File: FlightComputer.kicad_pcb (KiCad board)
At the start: 2 copper layers, 73.7 x 73.7 mm, 88 parts, among them J1 B3B-XH-A, J3 DM3D-SF, J4 12401832E402A, U1 AP62150WU-7TSOT26-WU_DIO, U2 TPS2121RUXR, U4 RP2350_60QFN, Y1 ABM8-272-T3

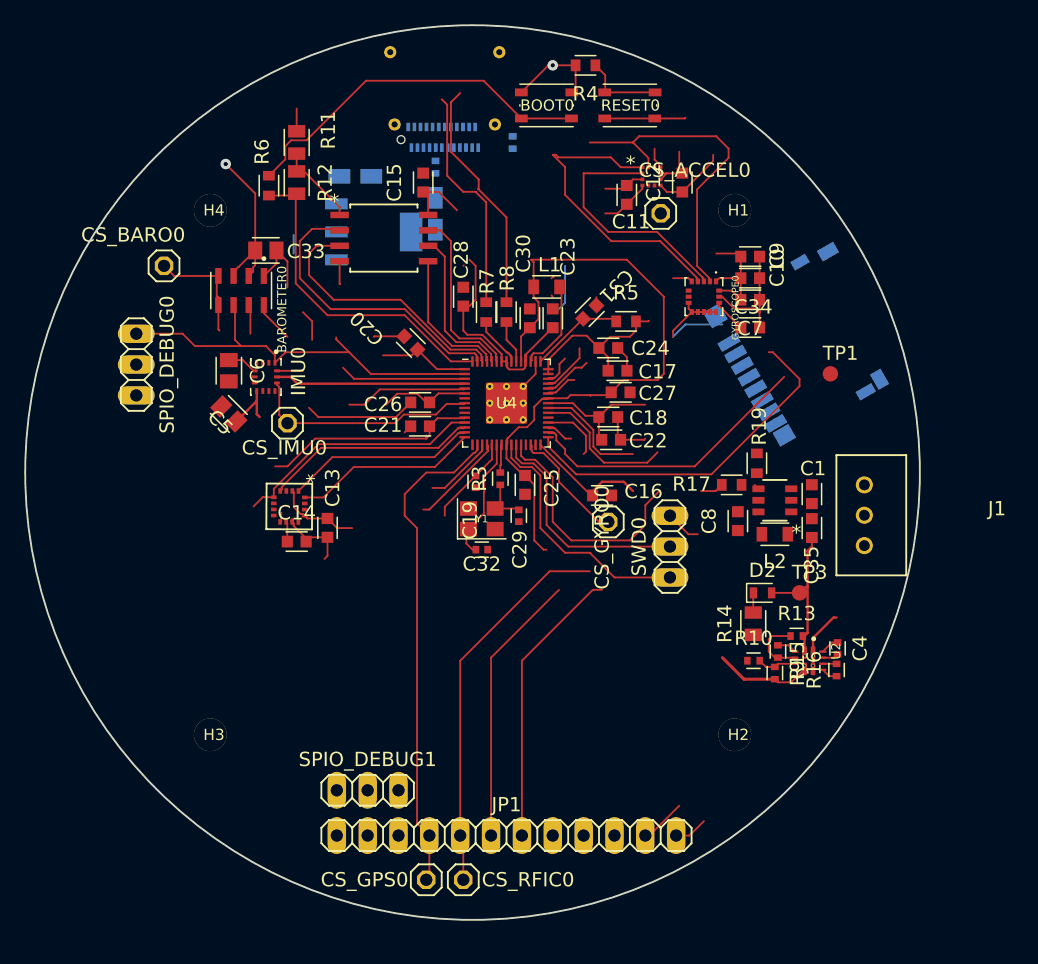
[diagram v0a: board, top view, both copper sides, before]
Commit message: fix: derived + added missing vals for passives, cleaned up stuff
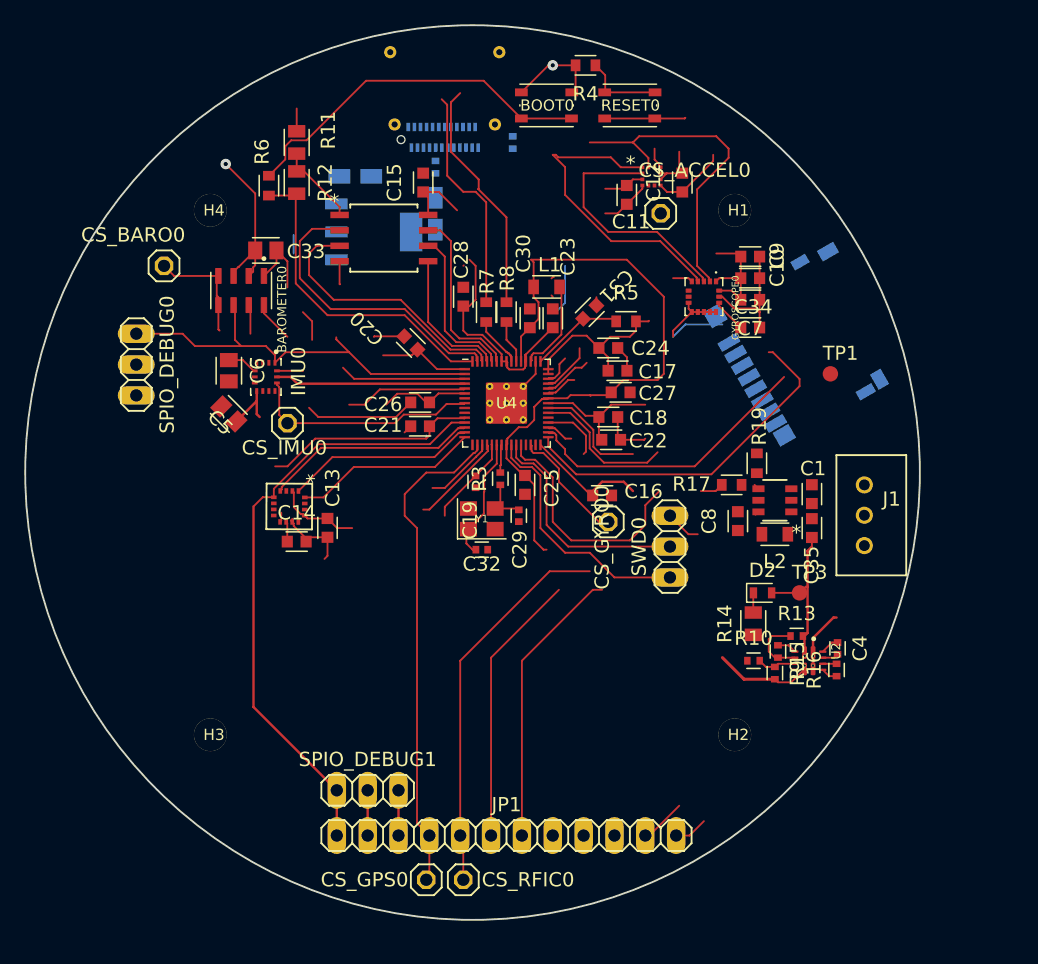
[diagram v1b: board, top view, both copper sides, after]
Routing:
- net MISO1: track 20.7 -> 50.6 mm
- net MOSI1: track 15.2 -> 18.9 mm
- net SCLK1: track 15.7 -> 19.4 mm
- added copper zone on In2.Cu, net +3.3V
- added copper zone on In1.Cu, net GND
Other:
- copper layers 2 -> 4
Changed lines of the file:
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@@
 	(layers
 		(0 "F.Cu" signal)
+		(4 "In1.Cu" signal)
+		(6 "In2.Cu" signal)
 		(2 "B.Cu" signal)
 		(9 "F.Adhes" user "F.Adhesive")
@@
 	)
 	(setup
+		(stackup
+			(layer "F.SilkS"
+				(type "Top Silk Screen")
+			)
+			(layer "F.Paste"
+				(type "Top Solder Paste")
+			)
+			(layer "F.Mask"
+				(type "Top Solder Mask")
+				(thickness 0.01)
+			)
+			(layer "F.Cu"
+				(type "copper")
+				(thickness 0.035)
+			)
+			(layer "dielectric 1"
+				(type "prepreg")
+				(thickness 0.1)
+				(material "FR4")
+				(epsilon_r 4.5)
+				(loss_tangent 0.02)
+			)
+			(layer "In1.Cu"
+				(type "copper")
+				(thickness 0.035)
+			)
+			(layer "dielectric 2"
+				(type "core")
+				(thickness 1.24)
+				(material "FR4")
+				(epsilon_r 4.5)
+				(loss_tangent 0.02)
+			)
+			(layer "In2.Cu"
+				(type "copper")
+				(thickness 0.035)
+			)
+			(layer "dielectric 3"
+				(type "prepreg")
+				(thickness 0.1)
+				(material "FR4")
+				(epsilon_r 4.5)
+				(loss_tangent 0.02)
+			)
+			(layer "B.Cu"
+				(type "copper")
+				(thickness 0.035)
+			)
+			(layer "B.Mask"
+				(type "Bottom Solder Mask")
+				(thickness 0.01)
+			)
+			(layer "B.Paste"
+				(type "Bottom Solder Paste")
+			)
+			(layer "B.SilkS"
+				(type "Bottom Silk Screen")
+			)
+			(copper_finish "None")
+			(dielectric_constraints no)
+		)
 		(pad_to_mask_clearance 0)
 		(allow_soldermask_bridges_in_footprints no)
@@
 		(at 180.7591 106.0196 -90)
 		(property "Reference" "J1"
-			(at 1.27 -10.922 0)
+			(at 0.4804 -2.2409 0)
 			(unlocked yes)
 			(layer "F.SilkS")
@@
 		(descr "Chip, 2.00 X 1.25 X 1.10 mm body\n\nChip package with body size 2.00 X 1.25 X 1.10 mm")
 		(property "Reference" "C5"
-			(at 0.000001 -1.681701 -45)
+			(at 0.000001 -1.681701 315)
 			(unlocked yes)
 			(layer "F.SilkS")
@@
 		)
 		(property "Value" ""
-			(at 0.000001 1.681701 -45)
+			(at 0.000001 1.681701 315)
 			(unlocked yes)
 			(layer "F.Fab")
@@
 		(descr "Chip, 1.60 X 0.80 X 0.85 mm body\n\nChip package with body size 1.60 X 0.80 X 0.85 mm")
 		(property "Reference" "C31"
-			(at -3.053284 0.653166 -135)
+			(at -3.053284 0.653166 225)
 			(unlocked yes)
 			(layer "F.SilkS")
@@
 		)
 		(property "Value" ""
-			(at 0.000003 1.681701 -135)
+			(at 0.000003 1.681701 225)
 			(unlocked yes)
 			(layer "F.Fab")
@@
 		)
 		(property "Value" "KX134-1211LGA12_2X2X0P9_ROM"
-			(at -1.7288 0.635 0)
+			(at -3.2331 0.635 0)
 			(unlocked yes)
 			(layer "F.Fab")
@@
 		(at 133.41245 107.7976 -90.3)
 		(property "Reference" "MAGNETOMETER0"
-			(at -3.271195 0.63503 -179.7)
+			(at -3.271195 0.63503 180.3)
 			(unlocked yes)
 			(layer "F.Fab")
@@
 		)
 		(property "Value" "MMC5983MAMMC5983MA_MEM"
-			(at -1.728787 0.635029 -179.7)
+			(at -1.728787 0.635029 180.3)
 			(unlocked yes)
 			(layer "F.Fab")
@@
 		(descr "Chip, 1.60 X 0.80 X 0.85 mm body\n\nChip package with body size 1.60 X 0.80 X 0.85 mm")
 		(property "Reference" "C20"
-			(at -3.412499 1.012376 -225)
+			(at -3.412499 1.012376 135)
 			(unlocked yes)
 			(layer "F.SilkS")
@@
 		)
 		(property "Value" ""
-			(at 0.000001 1.681699 -225)
+			(at 0.000001 1.681699 135)
 			(unlocked yes)
 			(layer "F.Fab")
@@
 		)
 		(property "Datasheet" ""
-			(at 0 0 -60)
+			(at 0 0 300)
 			(layer "B.Fab")
 			(hide yes)
@@
 		)
 		(property "Description" ""
-			(at 0 0 -60)
+			(at 0 0 300)
 			(layer "B.Fab")
 			(hide yes)
@@
 		(descr "Chip, 1.05 X 0.54 X 0.40 mm body\n\nChip package with body size 1.05 X 0.54 X 0.40 mm")
 		(property "Reference" "R18"
-			(at -2.794 0.508 -90)
+			(at -2.794 0.508 270)
 			(unlocked yes)
 			(layer "B.SilkS")
@@
 		)
 		(property "Value" "5.1k"
-			(at 0 -2.54 -90)
+			(at 0 -2.54 270)
 			(unlocked yes)
 			(layer "B.Fab")
@@
 		)
 		(property "Datasheet" ""
-			(at 0 0 -90)
+			(at 0 0 270)
 			(layer "B.Fab")
 			(hide yes)
@@
 		)
 		(property "Description" ""
-			(at 0 0 -90)
+			(at 0 0 270)
 			(layer "B.Fab")
 			(hide yes)
@@
 		(descr "Chip, 1.05 X 0.54 X 0.40 mm body\n\nChip package with body size 1.05 X 0.54 X 0.40 mm")
 		(property "Reference" "R20"
-			(at -3.302 0.508 -90)
+			(at -3.302 0.508 270)
 			(unlocked yes)
 			(layer "B.SilkS")
@@
 		)
 		(property "Value" "5.1k"
-			(at 0 -2.54 -90)
+			(at 0 -2.54 270)
 			(unlocked yes)
 			(layer "B.Fab")
@@
 		)
 		(property "Datasheet" ""
-			(at 0 0 -90)
+			(at 0 0 270)
 			(layer "B.Fab")
 			(hide yes)
@@
 		)
 		(property "Description" ""
-			(at 0 0 -90)
+			(at 0 0 270)
 			(layer "B.Fab")
 			(hide yes)
@@
 		(descr "Molded Body, 3.20 X 1.60 X 1.80 mm body\n\nMolded Body package with body size 3.20 X 1.60 X 1.80 mm")
 		(property "Reference" "C3"
-			(at 1.524 -1.27 -90)
+			(at 1.524 -1.27 270)
 			(unlocked yes)
 			(layer "B.SilkS")
@@
 		)
 		(property "Value" "100u"
-			(at 0 -2.54 -90)
+			(at 0 -2.54 270)
 			(unlocked yes)
 			(layer "B.Fab")
@@
 		)
 		(property "Datasheet" ""
-			(at 0 0 -90)
+			(at 0 0 270)
 			(layer "B.Fab")
 			(hide yes)
@@
 		)
 		(property "Description" ""
-			(at 0 0 -90)
+			(at 0 0 270)
 			(layer "B.Fab")
 			(hide yes)
@@
 	)
 	(segment
+		(start 139.8651 134.890806)
+		(end 139.8651 131.1656)
+		(width 0.2)
+		(layer "F.Cu")
+		(net 26)
+	)
+	(segment
 		(start 147.8576 102.0886)
 		(end 145.3998 104.5464)
@@
 	)
 	(segment
+		(start 137.3251 131.1656)
+		(end 130.4671 124.3076)
+		(width 0.2)
+		(layer "F.Cu")
+		(net 41)
+	)
+	(segment
 		(start 132.141394 107.0356)
 		(end 132.141394 106.34185)
@@
 	)
 	(segment
+		(start 137.3251 134.890806)
+		(end 137.3251 131.1656)
+		(width 0.2)
+		(layer "F.Cu")
+		(net 41)
+	)
+	(segment
 		(start 132.141394 106.34185)
 		(end 135.816444 102.6668)
@@
 	)
 	(segment
+		(start 130.4671 124.3076)
+		(end 130.4671 107.7976)
+		(width 0.2)
+		(layer "F.Cu")
+		(net 41)
+	)
+	(segment
 		(start 143.9291 133.874806)
 		(end 143.9291 109.5756)
@@
 	)
 	(segment
+		(start 142.4051 134.890806)
+		(end 142.4051 131.1656)
+		(width 0.2)
+		(layer "F.Cu")
+		(net 43)
+	)
+	(segment
 		(start 147.340057 101.76)
 		(end 145.366457 103.7336)
@@
 		(net 72)
 	)
+	(zone
+		(net 1)
+		(net_name "GND")
+		(layer "In1.Cu")
+		(hatch edge 0.5)
+		(connect_pads
+			(clearance 0.5)
+		)
+		(min_thickness 0.25)
+		(filled_areas_thickness no)
+		(fill yes
+			(thermal_gap 0.5)
+			(thermal_bridge_width 0.5)
+		)
+		(polygon
+			(pts
+				(xy 104 68) (xy 183 67.5) (xy 191 144.5) (xy 107 145)
+			)
+		)
+	)
+	(zone
+		(net 47)
+		(net_name "+3.3V")
+		(layer "In2.Cu")
+		(hatch edge 0.5)
+		(priority 1)
+		(connect_pads
+			(clearance 0.5)
+		)
+		(min_thickness 0.25)
+		(filled_areas_thickness no)
+		(fill yes
+			(thermal_gap 0.5)
+			(thermal_bridge_width 0.5)
+		)
+		(polygon
+			(pts
+				(xy 110 68) (xy 187 68.5) (xy 187.5 144.5) (xy 111.5 144.5)
+			)
+		)
+	)
 	(embedded_fonts no)

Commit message: fix: cleaned up schematic + pcb footprints
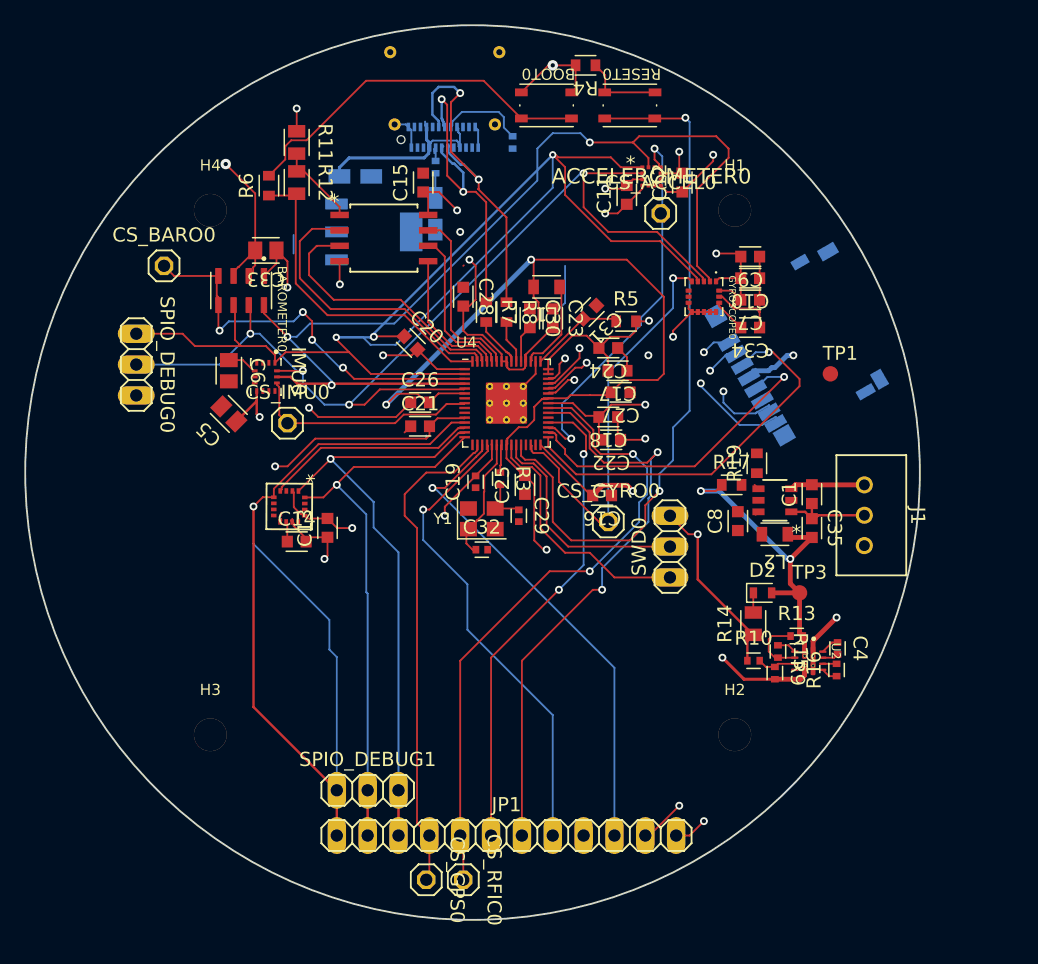
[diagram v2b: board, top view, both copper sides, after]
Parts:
- ACCELEROMETER0: footprint LGA12_2X2X0P9_ROM -> FlightComputer:LGA12_2X2X0P9_ROM
- BAROMETER0: footprint SON125P300X500X100-8N -> FlightComputer:SON125P300X500X100-8N
- BOOT0, RESET0: footprint BUTTON_SWITCH_SMD_SW_PUSH_1P1T_NO_VERTICAL_WUERTH_434133025816 -> FlightComputer:BUTTON_SWITCH_SMD_SW_PUSH_1P1T_NO_VERTICAL_WUERTH_434133025816
- C1, C14: value (none) -> 10uF; footprint CAPC1608X85 -> FlightComputer:CAPC1608X85
- C10: value (none) -> 2.2uF; footprint CAPC1608X85 -> FlightComputer:CAPC1608X85
- C11, C12, C9: value (none) -> 0.1uF; footprint CAPC1608X85 -> FlightComputer:CAPC1608X85
- C13: value (none) -> 1uF; footprint CAPC1608X85 -> FlightComputer:CAPC1608X85
- C15, C8: value (none) -> 100nF; footprint CAPC1608X85 -> FlightComputer:CAPC1608X85
- C16, C17, C18, C20, C21, C22, C23, C24, C25, C27: value (none) -> 100n; footprint CAPC1608X85 -> FlightComputer:CAPC1608X85
- C19: value (none) -> 100n; footprint CAPC1005X60 -> FlightComputer:CAPC1005X60
- C2, C3: footprint CAPMP3216X180N -> FlightComputer:CAPMP3216X180N
- C26, C28, C31: value (none) -> 4.7u; footprint CAPC1608X85 -> FlightComputer:CAPC1608X85
- C29, C32: value (none) -> 15pF; footprint CAPC1005X60 -> FlightComputer:CAPC1005X60
- C30: value (none) -> 1.7u; footprint CAPC1608X85 -> FlightComputer:CAPC1608X85
- C33: value (none) -> 100nF; footprint CAPC2012X110 -> FlightComputer:CAPC2012X110
- C34: value (none) -> 0.47uF; footprint CAPC1608X85 -> FlightComputer:CAPC1608X85
- C35: value (none) -> 22uF; footprint CAPC1608X85 -> FlightComputer:CAPC1608X85
- C4: footprint CAPC1005X60 -> FlightComputer:CAPC1005X60
- C5, C6: value (none) -> 0.1u; footprint CAPC2012X110 -> FlightComputer:CAPC2012X110
- C7: value (none) -> 10nF; footprint CAPC1608X85 -> FlightComputer:CAPC1608X85
- CS_ACCEL0, CS_BARO0, CS_GPS0, CS_GYRO0, CS_IMU0, CS_RFIC0: footprint 1X01 -> FlightComputer:1X01
- D2: value CHIP-FLAT-B_0603-0.35MM -> LED; footprint LEDC1608X35N_FLAT-B -> FlightComputer:LEDC1608X35N_FLAT-B
- FLASH_MEMORY0: footprint SOIC-8_5P28X5P28_WIN -> FlightComputer:SOIC-8_5P28X5P28_WIN
- GYROSCOPE0: footprint PQFN50P300X300X80-16N -> FlightComputer:PQFN50P300X300X80-16N
- H1, H2, H3, H4: footprint MOUNTINGHOLE_MOUNTINGHOLE_2.7MM_M2.5 -> FlightComputer:MOUNTINGHOLE_MOUNTINGHOLE_2.7MM_M2.5
- IMU0: footprint IC_ICM-45686 -> FlightComputer:IC_ICM-45686
- J1: footprint B3B-XH-A -> FlightComputer:B3B-XH-A
- J3: footprint HRS_DM3D-SF -> FlightComputer:HRS_DM3D-SF
- J4: footprint 12401832E402A -> FlightComputer:12401832E402A
- JP1: footprint 1X12 -> FlightComputer:1X12
- L1: value (none) -> 3.3u; footprint INDC2009X120 -> FlightComputer:INDC2009X120
- L2: value (none) -> 3.3uH; footprint INDC2009X120 -> FlightComputer:INDC2009X120
- MAGNETOMETER0: footprint MMC5983MA_MEM -> FlightComputer:MMC5983MA_MEM
- R10, R13, R15, R16, R18, R20, R9: footprint RESC1005X40 -> FlightComputer:RESC1005X40
- R11: value (none) -> 10k; footprint RESC2012X65 -> FlightComputer:RESC2012X65
- R12: value (none) -> 0k; footprint RESC2012X65 -> FlightComputer:RESC2012X65
- R14: value (none) -> 1k; footprint RESC2012X65 -> FlightComputer:RESC2012X65
- R17: footprint RESC1608X60 -> FlightComputer:RESC1608X60
- R19: value (none) -> 10k; footprint RESC1608X60 -> FlightComputer:RESC1608X60
- R3: value (none) -> 1k; footprint RESC1005X40 -> FlightComputer:RESC1005X40
- R4, R6: value (none) -> 1k; footprint RESC1608X60 -> FlightComputer:RESC1608X60
- R5: value (none) -> 3.3; footprint RESC1608X60 -> FlightComputer:RESC1608X60
- R7, R8: value (none) -> 27; footprint RESC1608X60 -> FlightComputer:RESC1608X60
- SPIO_DEBUG0, SPIO_DEBUG1, SWD0: footprint 1X03 -> FlightComputer:1X03
- TP1, TP3: footprint B1,27 -> FlightComputer:B1,27
- U1: footprint TSOT26-WU_DIO -> FlightComputer:TSOT26-WU_DIO
- U2: footprint IC_TPS2121RUXR -> FlightComputer:IC_TPS2121RUXR
- U4: footprint RP2350_60QFN_MINIMAL_RP2350-QFN-60-1EP_7X7_P0.4MM_EP3.4X3.4MM_THERMALVIAS -> FlightComputer:RP2350_60QFN_MINIMAL_RP2350-QFN-60-1EP_7X7_P0.4MM_EP3.4X3.4MM_THERMALVIAS
- VR1: footprint SOT230P700X170-4 -> FlightComputer:SOT230P700X170-4
- Y1: footprint CRYSTAL_CRYSTAL_SMD_3225-4PIN_3.2X2.5MM -> FlightComputer:CRYSTAL_CRYSTAL_SMD_3225-4PIN_3.2X2.5MM
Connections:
- net +3V3_USB renamed /+3V3_USB
- net +3V3_VBAT renamed /+3V3_VBAT
- net +7.4V renamed /+7.4V
- net CS_ACCEL renamed /CS_ACCEL
- net CS_BARO renamed /CS_BARO
- net CS_GPS renamed /CS_GPS
- net CS_GYRO renamed /CS_GYRO
- net CS_IMU renamed /CS_IMU
- net CS_MAG renamed /CS_MAG
- net CS_RFIC renamed /CS_RFIC
- net GPIO12 renamed /GPIO12
- net GPIO16 renamed /GPIO16
- net GPIO23 renamed /GPIO23
- net GPIO4 renamed /GPIO4
- net GPIO7 renamed /GPIO7
- net LNA_EN_LP renamed /LNA_EN_LP
- net MISO0 renamed /MISO0
- net MISO1 renamed /MISO1
- net MOSI0 renamed /MOSI0
- net MOSI1 renamed /MOSI1
- net PA_EN_LP renamed /PA_EN_LP
- net QSPI_SCLK renamed /QSPI_SCLK
- net QSPI_SD0 renamed /QSPI_SD0
- net QSPI_SD1 renamed /QSPI_SD1
- net QSPI_SD2 renamed /QSPI_SD2
- net QSPI_SD3 renamed /QSPI_SD3
- net QSPI_SS renamed /QSPI_SS
- net RF_GPIO0 renamed /RF_GPIO0
- net RF_GPIO2 renamed /RF_GPIO2
- net RF_GPIO3 renamed /RF_GPIO3
- net RUN renamed /RUN
- net SCLK0 renamed /SCLK0
- net SCLK1 renamed /SCLK1
- net SDIO_CLK renamed /SDIO_CLK
- net SDIO_CMD renamed /SDIO_CMD
- net SDIO_D0 renamed /SDIO_D0
- net SDIO_D1 renamed /SDIO_D1
- net SDIO_D2 renamed /SDIO_D2
- net SDIO_D3 renamed /SDIO_D3
- net SWCLK renamed /SWCLK
- net SWD renamed /SWD
- net USB_N renamed /USB_N
- net USB_OUT_N renamed /USB_OUT_N
- net USB_OUT_P renamed /USB_OUT_P
- net USB_P renamed /USB_P
- net VREG_AVDD renamed /VREG_AVDD
- net VREG_LX renamed Net-(U4-VREG_LX)
- net V_USB renamed /V_USB
- net XIN renamed /XIN
- net XOUT renamed /XOUT
- net ~{USB_BOOT} renamed /~{USB_BOOT}
- ACCELEROMETER0 pad 11: (no net) -> unconnected-(ACCELEROMETER0-NC-Pad11)
- ACCELEROMETER0 pad 5: (no net) -> unconnected-(ACCELEROMETER0-INT1-Pad5)
- ACCELEROMETER0 pad 6: (no net) -> unconnected-(ACCELEROMETER0-INT2-Pad6)
- C6 pad 1: +3.3V -> +3V3
- GYROSCOPE0 pad 6: (no net) -> unconnected-(GYROSCOPE0-INT-Pad6)
- GYROSCOPE0 pad 7: (no net) -> unconnected-(GYROSCOPE0-RESV7-Pad7)
- IMU0 pad 10: (no net) -> unconnected-(IMU0-RESV/AUX1_CS-Pad10)
- IMU0 pad 11: (no net) -> unconnected-(IMU0-RESV/AUX1_SDO-Pad11)
- IMU0 pad 2: (no net) -> unconnected-(IMU0-RESV/AUX1_SDIO/AUX1_SDI/MAS_DA-Pad2)
- IMU0 pad 3: (no net) -> unconnected-(IMU0-RESV/AUX1_SCLK/MAS_CLK-Pad3)
- IMU0 pad 4: (no net) -> unconnected-(IMU0-INT1/INT-Pad4)
- IMU0 pad 5: +3.3V -> +3V3
- IMU0 pad 7: (no net) -> unconnected-(IMU0-RESV-Pad7)
- IMU0 pad 9: (no net) -> unconnected-(IMU0-INT2/FSYNC/CLKIN-Pad9)
- J1 pad 3: (no net) -> unconnected-(J1-Pad3)
- J3 pad S1: (no net) -> Net-(J3-SHIELD-PadS1)
- J3 pad S2: (no net) -> Net-(J3-SHIELD-PadS1)
- J3 pad S3: (no net) -> Net-(J3-SHIELD-PadS1)
- J3 pad S4: (no net) -> Net-(J3-SHIELD-PadS1)
- J3 pad SW-A: (no net) -> unconnected-(J3-PadSW-A)
- J3 pad SW-B: (no net) -> unconnected-(J3-PadSW-B)
- J4 pad A10: (no net) -> unconnected-(J4-RX2--PadA10)
- J4 pad A11: (no net) -> unconnected-(J4-RX2+-PadA11)
- J4 pad A2: (no net) -> unconnected-(J4-TX1+-PadA2)
- J4 pad A3: (no net) -> unconnected-(J4-TX1--PadA3)
- J4 pad A8: (no net) -> unconnected-(J4-SBU1-PadA8)
- J4 pad B10: (no net) -> unconnected-(J4-RX1--PadB10)
- J4 pad B11: (no net) -> unconnected-(J4-RX1+-PadB11)
- J4 pad B2: (no net) -> unconnected-(J4-TX2+-PadB2)
- J4 pad B3: (no net) -> unconnected-(J4-TX2--PadB3)
- J4 pad B8: (no net) -> unconnected-(J4-SBU2-PadB8)
- MAGNETOMETER0 pad 12: (no net) -> unconnected-(MAGNETOMETER0-NC_6-Pad12)
- MAGNETOMETER0 pad 14: (no net) -> unconnected-(MAGNETOMETER0-NC-Pad14)
- MAGNETOMETER0 pad 15: (no net) -> unconnected-(MAGNETOMETER0-INT-Pad15)
- MAGNETOMETER0 pad 3: (no net) -> unconnected-(MAGNETOMETER0-NC_2-Pad3)
- MAGNETOMETER0 pad 6: (no net) -> unconnected-(MAGNETOMETER0-NC_3-Pad6)
- MAGNETOMETER0 pad 7: (no net) -> unconnected-(MAGNETOMETER0-NC_4-Pad7)
- MAGNETOMETER0 pad 8: (no net) -> unconnected-(MAGNETOMETER0-NC_5-Pad8)
- R17 pad 2: N$12 -> Net-(R17-Pad2)
- R19 pad 1: N$12 -> Net-(R17-Pad2)
- TP1 pad TP: N$2 -> unconnected-(TP1-PadTP)
- U1 pad 4: N$12 -> unconnected-(U1-FB-Pad4)
- U1 pad 5: (no net) -> unconnected-(U1-EN-Pad5)
- U4 pad 29: (no net) -> unconnected-(U4-GPIO18-Pad29)
- U4 pad 9: CS -> unconnected-(U4-GPIO6-Pad9)
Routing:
- net MISO0: track 0.00 -> 110.5 mm
- net SCLK0: track 0.00 -> 85.4 mm
- net /MISO0: track 60.3 -> 0.00 mm, vias 0 -> 2
- net /MOSI0: track 34.8 -> 83.9 mm, vias 0 -> 4
- net /SCLK0: track 46.2 -> 0.00 mm, vias 0 -> 3
- net /LNA_EN_LP: track 5.84 -> 40.8 mm, vias 0 -> 1
- net /SCLK1: track 19.4 -> 52.7 mm, vias 0 -> 1
- net /RUN: track 26.6 -> 58.5 mm, vias 0 -> 2
- net /RF_GPIO3: track 7.86 -> 39.1 mm, vias 0 -> 1
- net /MISO1: track 50.6 -> 80.5 mm, vias 0 -> 1
- net /MOSI1: track 18.9 -> 48.9 mm, vias 0 -> 1
- net /CS_ACCEL: track 4.02 -> 32.1 mm, vias 0 -> 2
- net /CS_GYRO: track 11.6 -> 33.8 mm, vias 0 -> 1
- net GND: track 97.2 -> 118.5 mm, vias 2 -> 13
- net +1V1: track 61.8 -> 78.6 mm, vias 0 -> 3
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- added copper zone on In2.Cu, net +3V3
- removed copper zone on In2.Cu, net +3.3V

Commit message: version that newbies can play with
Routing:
- net /SDIO_D2: track 6.67 -> 21.7 mm, vias 2 -> 5
- net GND: vias 13 -> 12
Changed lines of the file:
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@@
 		(descr "Chip, 1.05 X 0.54 X 0.40 mm body\n\nChip package with body size 1.05 X 0.54 X 0.40 mm")
 		(property "Reference" "R3"
-			(at 0 -2.54 270)
+			(at -1.5116 -3.7129 0)
 			(unlocked yes)
 			(layer "F.SilkS")
@@
 		(descr "Chip, 1.60 X 0.80 X 0.85 mm body\n\nChip package with body size 1.60 X 0.80 X 0.85 mm")
 		(property "Reference" "C14"
-			(at 0 -2.54 0)
+			(at -0.0231 1.31135 0)
 			(unlocked yes)
 			(layer "F.SilkS")
@@
 		)
 		(property "Datasheet" ""
-			(at 0 0 269.7)
+			(at 0 0 89.7)
 			(layer "F.Fab")
 			(hide yes)
@@
 		)
 		(property "Description" ""
-			(at 0 0 269.7)
+			(at 0 0 89.7)
 			(layer "F.Fab")
 			(hide yes)
@@
 			)
 		)
+		(property "Name" "${REFERENCE}"
+			(at -2.79802 -0.072901 0)
+			(unlocked yes)
+			(layer "F.SilkS")
+			(effects
+				(font
+					(size 1 1)
+					(thickness 0.15)
+				)
+			)
+		)
 		(sheetname "/")
 		(sheetfile "FlightComputer.kicad_sch")
@@
 		(descr "Chip, 1.60 X 0.80 X 0.85 mm body\n\nChip package with body size 1.60 X 0.80 X 0.85 mm")
 		(property "Reference" "C25"
-			(at 0 -2.54 90)
+			(at 2.5196 -2.3191 0)
 			(unlocked yes)
 			(layer "F.SilkS")
@@
 		(descr "Chip, 1.00 X 0.50 X 0.60 mm body\n\nChip package with body size 1.00 X 0.50 X 0.60 mm")
 		(property "Reference" "C32"
-			(at 0 -2.54 0)
+			(at 0 1.1464 0)
 			(unlocked yes)
 			(layer "F.SilkS")
@@
 		(descr "Chip, 1.60 X 0.80 X 0.85 mm body\n\nChip package with body size 1.60 X 0.80 X 0.85 mm")
 		(property "Reference" "C13"
-			(at 0 -2.54 90)
+			(at 2.5597 1.94075 0)
 			(unlocked yes)
 			(layer "F.SilkS")
@@
 	)
 	(via
-		(at 162.9791 95.3516)
-		(size 0.65)
-		(drill 0.35)
-		(layers "F.Cu" "B.Cu")
-		(net 1)
-	)
-	(via
 		(at 159.4231 83.6676)
 		(size 0.65)
@@
 	)
 	(segment
+		(start 163.7205 92.376618)
+		(end 162.343882 91)
+		(width 0.2)
+		(layer "F.Cu")
+		(net 56)
+	)
+	(segment
+		(start 164.8753 95.0976)
+		(end 164.7777 95)
+		(width 0.2)
+		(layer "F.Cu")
+		(net 56)
+	)
+	(segment
 		(start 157.311225 94.763725)
 		(end 157.311225 95.587175)
@@
 	)
 	(segment
+		(start 163.7205 94)
+		(end 163.7205 92.376618)
+		(width 0.2)
+		(layer "F.Cu")
+		(net 56)
+	)
+	(segment
 		(start 157.311225 95.587175)
 		(end 155.2812 97.6172)
@@
 		(net 56)
 	)
+	(segment
+		(start 167.5511 95.0976)
+		(end 164.8753 95.0976)
+		(width 0.2)
+		(layer "F.Cu")
+		(net 56)
+	)
+	(segment
+		(start 162.343882 91)
+		(end 160 91)
+		(width 0.2)
+		(layer "F.Cu")
+		(net 56)
+	)
+	(via
+		(at 164.7777 95)
+		(size 0.6)
+		(drill 0.3)
+		(layers "F.Cu" "B.Cu")
+		(net 56)
+	)
+	(via
+		(at 160 91)
+		(size 0.6)
+		(drill 0.3)
+		(layers "F.Cu" "B.Cu")
+		(net 56)
+	)
 	(via
 		(at 157.3112 94.7637)
@@
 	)
 	(via
+		(at 163.7205 94)
+		(size 0.6)
+		(drill 0.3)
+		(layers "F.Cu" "B.Cu")
+		(net 56)
+	)
+	(via
 		(at 167.5511 95.0976)
 		(size 0.65)
@@
 		(layer "B.Cu")
 		(net 56)
+	)
+	(segment
+		(start 160 91)
+		(end 160 92.0749)
+		(width 0.2)
+		(layer "B.Cu")
+		(net 56)
+	)
+	(segment
+		(start 164.7777 95)
+		(end 164.7205 95)
+		(width 0.2)
+		(layer "B.Cu")
+		(net 56)
+	)
+	(segment
+		(start 160 92.0749)
+		(end 157.3112 94.7637)
+		(width 0.2)
+		(layer "B.Cu")
+		(net 56)
+	)
+	(segment
+		(start 164.7205 95)
+		(end 163.7205 94)
+		(width 0.2)
+		(layer "B.Cu")
+		(net 56)
